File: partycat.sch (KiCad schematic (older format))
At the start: 19 parts, among them P1 CONN_01X02, P2 CONN_01X03, P3 CONN_01X06, P4 CONN_01X06, P5 CONN_01X02, Q2 Q_NMOS_GDS, SW1 SW_PUSH, SW2 SW_PUSH, U1 AP1117, U2 ESP-12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

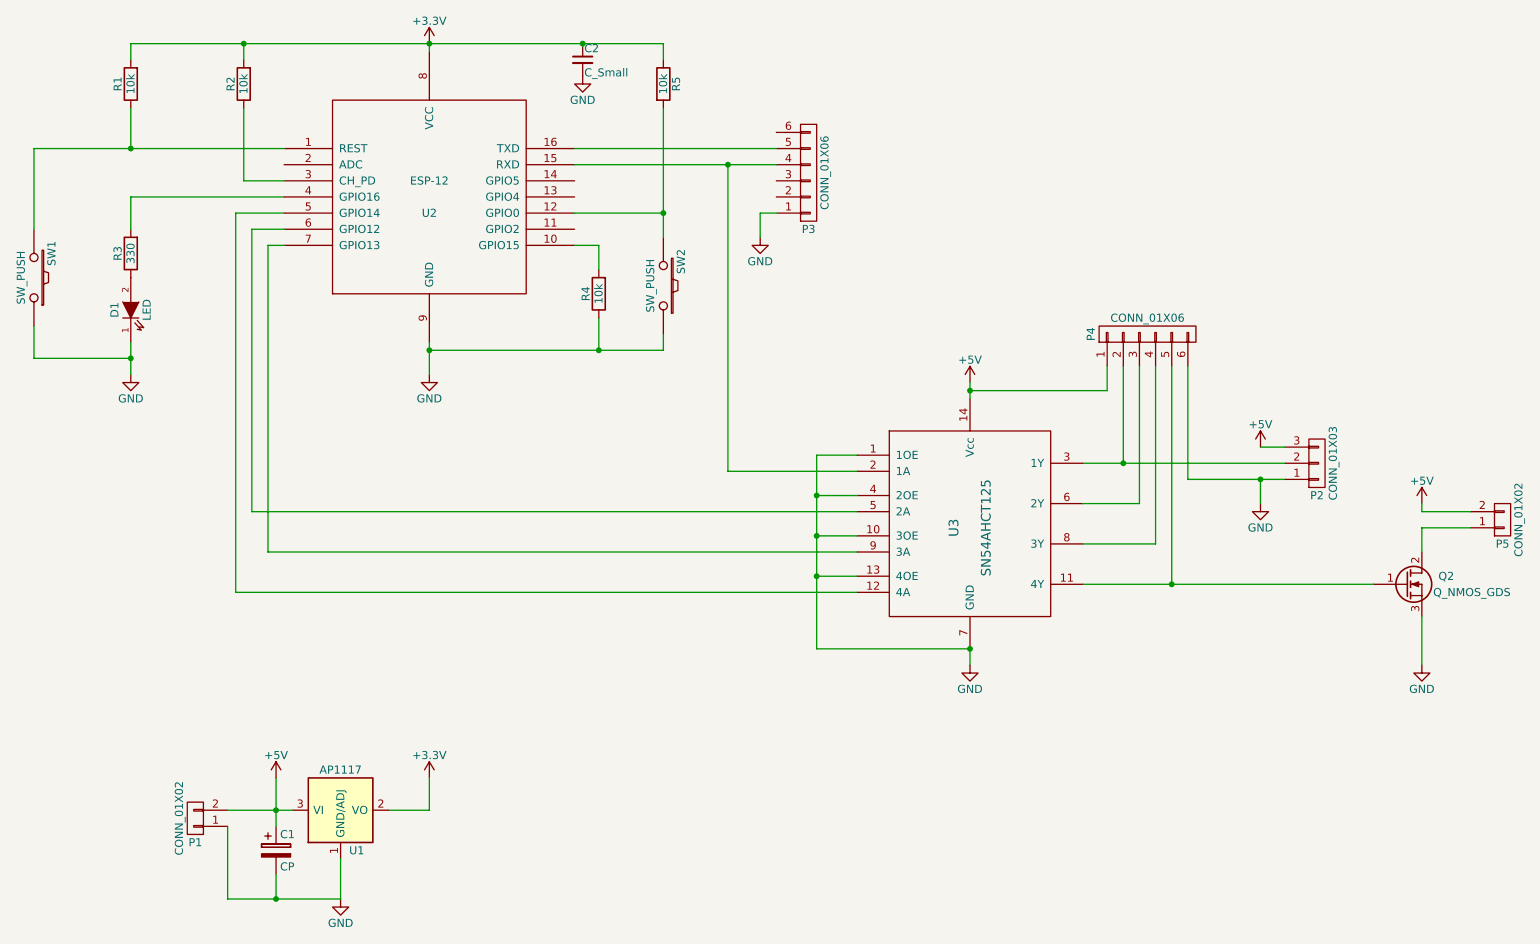
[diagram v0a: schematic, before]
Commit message: Added docs, panelized gerbers, and renamed files (all versions will use this repo)
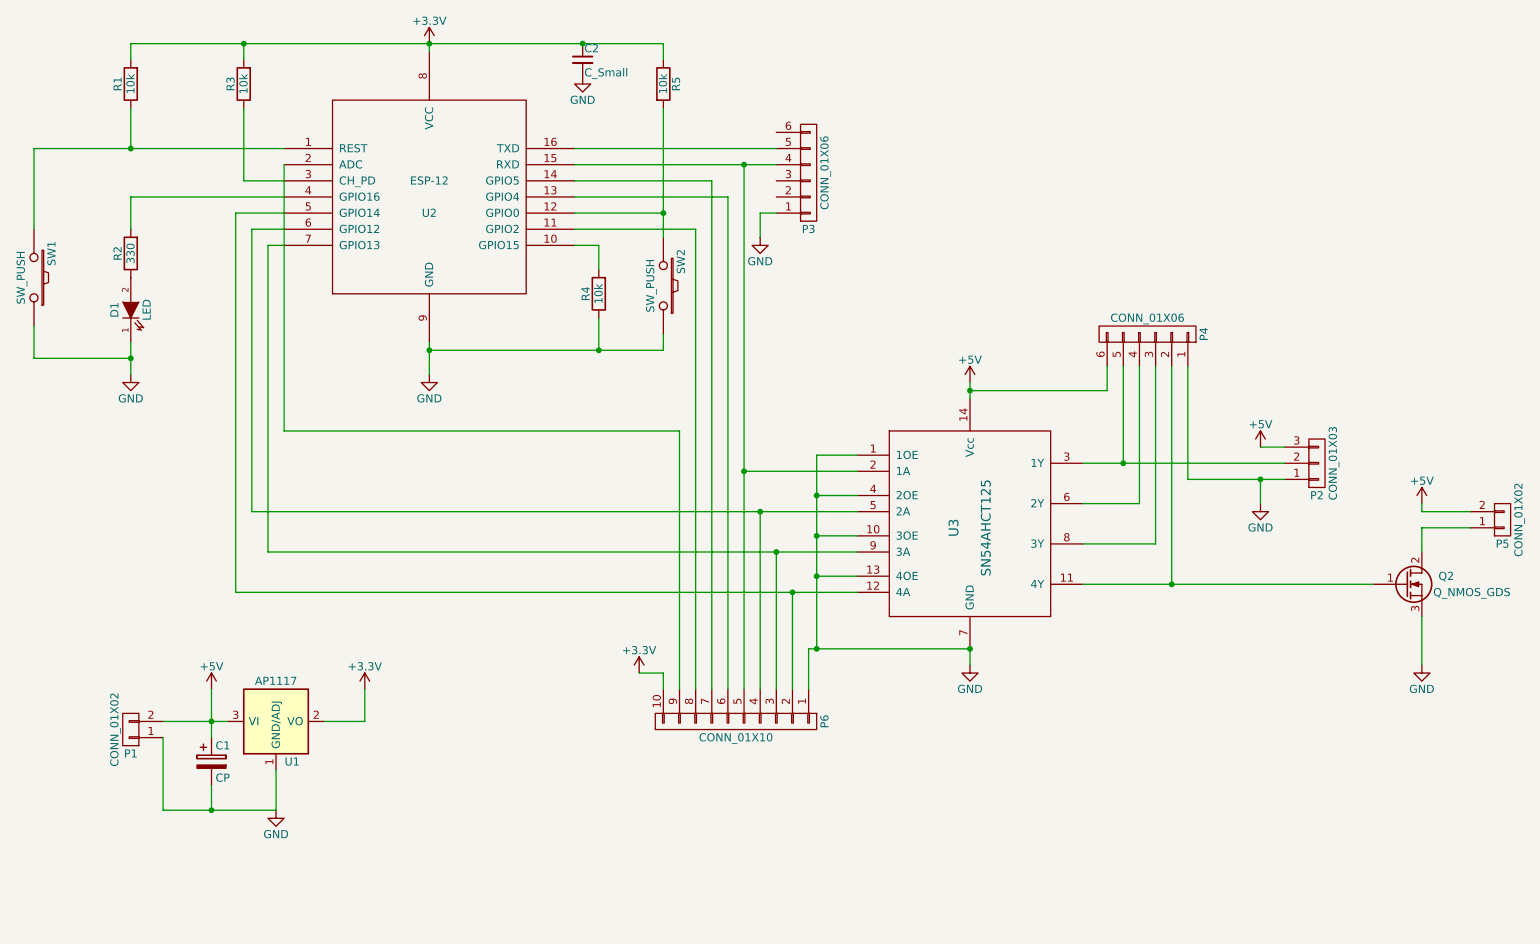
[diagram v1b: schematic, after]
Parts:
- added P6: CONN_01X10, Pin_Headers:Pin_Header_Straight_1x10, symbol CONN_01X10
- renumbered R3 to R2, R2 to R3
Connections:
- net +3V3: now also P6.10 (P10)
- net +5V: now also P4.6 (P6); no longer P4.1 (P1)
- net GND: now also P4.1 (P1), P6.1 (P1); no longer P4.6 (P6)
- net at P2.2 (P2), U3.3 (1Y): now also P4.5 (P5); no longer P4.2 (P2)
- net at Q2.1 (G), U3.11 (4Y): now also P4.2 (P2); no longer P4.5 (P5)
- net at U2.5 (GPIO14), U3.12 (4A): now also P6.2 (P2)
- net at P3.4 (P4), U2.15 (RXD), U3.2 (1A): now also P6.5 (P5)
- net at U2.6 (GPIO12), U3.5 (2A): now also P6.4 (P4)
- net at U3.6 (2Y): now also P4.4 (P4); no longer P4.3 (P3)
- net at U3.8 (3Y): now also P4.3 (P3); no longer P4.4 (P4)
- net at U2.7 (GPIO13), U3.9 (3A): now also P6.3 (P3)
- net at U2.11 (GPIO2): now also P6.8 (P8)
- net at U2.13 (GPIO4): now also P6.6 (P6)
- net at U2.14 (GPIO5): now also P6.7 (P7)
- net at U2.2 (ADC): now also P6.9 (P9)
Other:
- moved on the sheet: C1, P1, U1

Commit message: v4
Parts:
- removed P4: CONN_01X06, Pin_Headers:Pin_Header_Straight_1x06, symbol CONN_01X06
- removed P5: CONN_01X02, Terminal_Blocks:TerminalBlock_Pheonix_MKDS1.5-2pol, symbol CONN_01X02
- removed Q2: Q_NMOS_GDS, TO_SOT_Packages_THT:TO-220_Neutral123_Vertical, symbol Q_NMOS_GDS
- removed U3: SN54AHCT125, SMD_Packages:SSOP-14, symbol SN54AHCT125
- added C3: CP, Capacitors_THT:CP_Radial_D5.0mm_P2.50mm, symbol Device:CP
- added Q1: N-CH MOSFET, TO_SOT_Packages_SMD:SOT-23, symbol partycat-rescue:BSS138-RESCUE-partycat
- added R6: 4.7k, Resistors_SMD:R_0603_HandSoldering, symbol Device:R
- C1: footprint Capacitors_ThroughHole:C_Radial_D12.5_L25_P5 -> Capacitors_THT:CP_Radial_D12.5mm_P5.00mm; symbol CP -> Device:CP
- C2: symbol C_Small -> Device:C_Small
- D1: symbol LED -> Device:LED
- P1: symbol CONN_01X02 -> Connector:Screw_Terminal_01x02
- P2: symbol CONN_01X03 -> Connector_Generic:Conn_01x03
- P3: symbol CONN_01X06 -> Connector_Generic:Conn_01x06
- P6: symbol CONN_01X10 -> Connector_Generic:Conn_01x10
- R1, R2, R3, R4, R5: symbol R -> Device:R
- SW1, SW2: footprint Buttons_Switches_ThroughHole:SW_PUSH_SMALL -> Buttons_Switches_SMD:SW_SPST_PTS645; symbol SW_PUSH -> Switch:SW_Push
- U1: symbol AP1117 -> Regulator_Linear:AZ1117-3.3
- U2: symbol ESP-12 -> ESP8266:ESP-12
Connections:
- net +5V: now also C3.1, R6.2
- net GND: now also C3.2, Q1.2 (S)
- net at P2.2 (Pin_2): now also Q1.3 (D), R6.1
- net at P3.4 (Pin_4), P6.5 (Pin_5), U2.15 (RXD): now also Q1.1 (G)
- no-connect marks 0 -> 3
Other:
- moved on the sheet: U1
